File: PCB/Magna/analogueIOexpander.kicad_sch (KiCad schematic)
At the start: 2 parts, among them U1501 4052

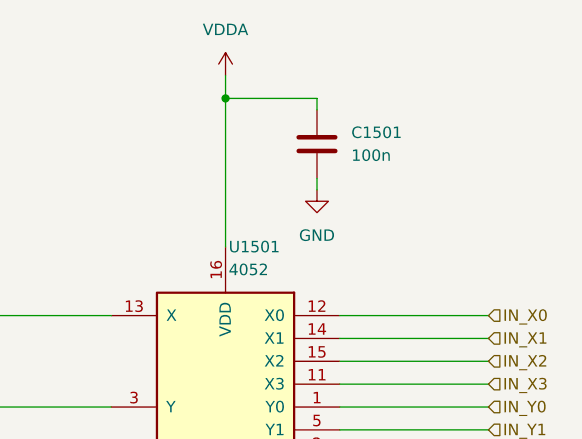
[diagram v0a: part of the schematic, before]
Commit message: Update capacitors to parts in JLC library
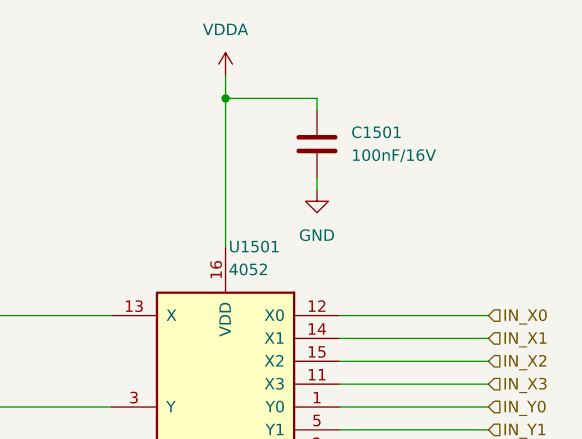
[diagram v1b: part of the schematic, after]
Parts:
- C1501: value 100n -> 100nF/16V; footprint (none) -> Capacitor_SMD:C_0805_2012Metric; LCSC (none) -> C218638
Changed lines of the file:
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@@
       (effects (font (size 1.27 1.27)) (justify left))
     )
-    (property "Value" "100n" (at 151.13 67.31 0)
+    (property "Value" "100nF/16V" (at 151.13 67.31 0)
       (effects (font (size 1.27 1.27)) (justify left))
     )
-    (property "Footprint" "" (at 148.2852 69.85 0)
+    (property "Footprint" "Capacitor_SMD:C_0805_2012Metric" (at 148.2852 69.85 0)
       (effects (font (size 1.27 1.27)) hide)
     )
@@
       (effects (font (size 1.27 1.27)) hide)
     )
+    (property "LCSC" "C218638" (at 147.32 66.04 0)
+      (effects (font (size 1.27 1.27)) hide)
+    )

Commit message: Select parts for all components
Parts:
- U1501: footprint (none) -> Package_SO:SO-16_3.9x9.9mm_P1.27mm; LCSC (none) -> C11350
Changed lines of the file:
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@@
       (effects (font (size 1.27 1.27)) (justify right))
     )
-    (property "Footprint" "" (at 137.16 100.33 0)
+    (property "Footprint" "Package_SO:SO-16_3.9x9.9mm_P1.27mm" (at 137.16 100.33 0)
       (effects (font (size 1.27 1.27)) hide)
     )
@@
       (effects (font (size 1.27 1.27)) hide)
     )
+    (property "LCSC" "C11350" (at 137.16 100.33 0)
+      (effects (font (size 1.27 1.27)) hide)
+    )

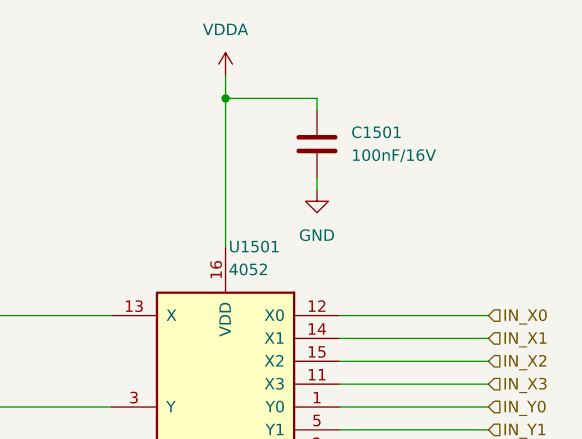
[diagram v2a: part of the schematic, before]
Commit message: Add even more component footprints and partnumbers
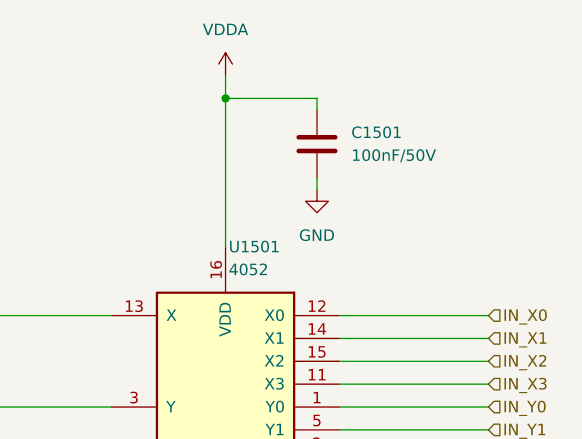
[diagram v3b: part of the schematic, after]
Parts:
- C1501: value 100nF/16V -> 100nF/50V; footprint Capacitor_SMD:C_0805_2012Metric -> Capacitor_SMD:C_0805_2012Metric_Pad1.18x1.45mm_HandSolder; LCSC C218638 -> C49678
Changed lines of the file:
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@@
       (effects (font (size 1.27 1.27)) (justify left))
     )
-    (property "Value" "100nF/16V" (at 151.13 67.31 0)
+    (property "Value" "100nF/50V" (at 151.13 67.31 0)
       (effects (font (size 1.27 1.27)) (justify left))
     )
-    (property "Footprint" "Capacitor_SMD:C_0805_2012Metric" (at 148.2852 69.85 0)
+    (property "Footprint" "Capacitor_SMD:C_0805_2012Metric_Pad1.18x1.45mm_HandSolder" (at 148.2852 69.85 0)
       (effects (font (size 1.27 1.27)) hide)
     )
@@
       (effects (font (size 1.27 1.27)) hide)
     )
-    (property "LCSC" "C218638" (at 147.32 66.04 0)
+    (property "LCSC" "C49678" (at 147.32 66.04 0)
       (effects (font (size 1.27 1.27)) hide)
     )
